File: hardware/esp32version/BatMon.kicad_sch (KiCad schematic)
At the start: 38 parts, among them J1 Battery_Connector, J3 Prog_Connector, J5 Charging_Connector, Q1 Q_PMOS_DDGSDD_TSOP-6, Q1 SS8050-G, Q2 Q_PMOS_DDGSDD_TSOP-6, Q2 SS8050-G, Q3 SS8050-G, SW1 POWER_SW, U1 ESP32-WROOM-32D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

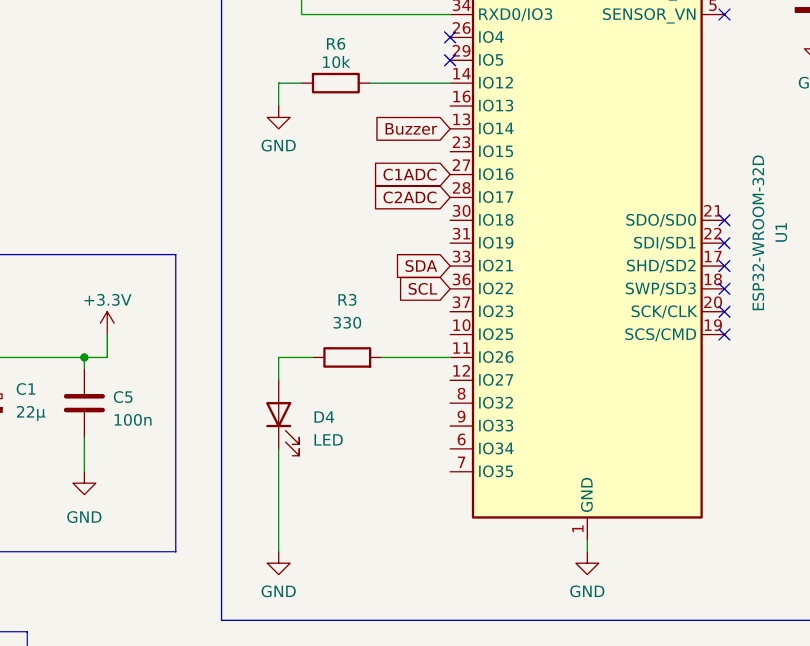
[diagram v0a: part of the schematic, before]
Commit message: fixed battery inputs being connected to non ADC pins on uC (new board revision)
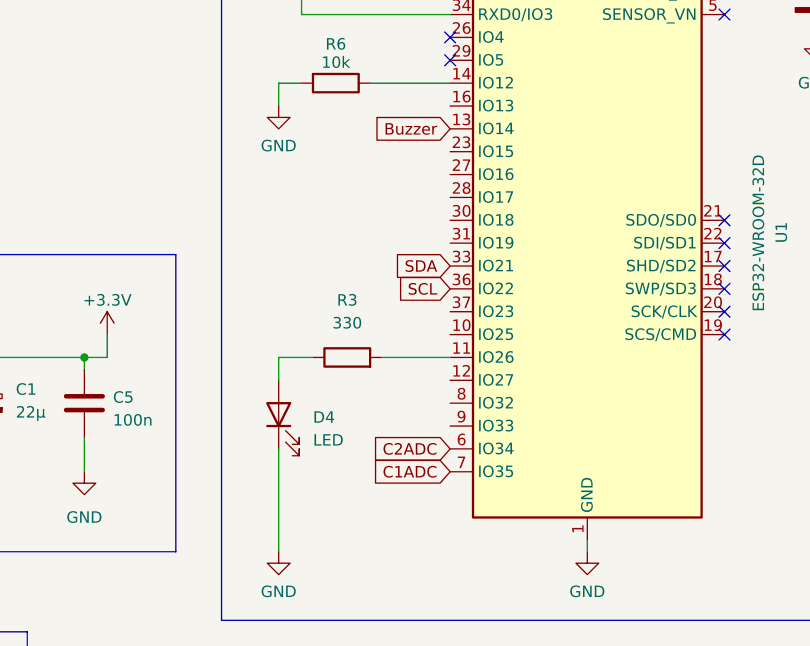
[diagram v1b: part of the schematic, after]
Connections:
- net C1ADC: now also U1.7 (IO35); no longer U1.27 (IO16)
- net C2ADC: now also U1.6 (IO34); no longer U1.28 (IO17)
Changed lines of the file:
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@@
     )
   )
-  (global_label "C2ADC" (shape input) (at 217.17 96.52 180) (fields_autoplaced)
+  (global_label "C2ADC" (shape input) (at 217.17 124.46 180) (fields_autoplaced)
     (effects (font (size 1.27 1.27)) (justify right))
-    (property "Intersheetrefs" "${INTERSHEET_REFS}" (at 208.1561 96.52 0)
+    (property "Intersheetrefs" "${INTERSHEET_REFS}" (at 208.1561 124.46 0)
       (effects (font (size 1.27 1.27)) (justify right) hide)
     )
@@
     )
   )
-  (global_label "C1ADC" (shape input) (at 217.17 93.98 180) (fields_autoplaced)
+  (global_label "C1ADC" (shape input) (at 217.17 127 180) (fields_autoplaced)
     (effects (font (size 1.27 1.27)) (justify right))
-    (property "Intersheetrefs" "${INTERSHEET_REFS}" (at 208.1561 93.98 0)
+    (property "Intersheetrefs" "${INTERSHEET_REFS}" (at 208.1561 127 0)
       (effects (font (size 1.27 1.27)) (justify right) hide)
     )

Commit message: updated programming connector to correct mouser component
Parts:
- J3: Part https://www.mouser.at/ProductDetail/Harwin/M50-3930542?qs=%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 -> https://www.mouser.at/ProductDetail/Harwin/M50-3930642?qs=%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
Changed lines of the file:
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@@
       (effects (font (size 1.27 1.27)) hide)
     )
-    (property "Datasheet" "https://www.mouser.at/ProductDetail/Harwin/M50-3930542?qs=%252BdQmOuGyFcFb1vakt822Tg%3D%3D" (at 226.06 31.75 0)
+    (property "Datasheet" "https://www.mouser.at/ProductDetail/Harwin/M50-3930642?qs=%252BdQmOuGyFcFzM9ygldPnXw%3D%3D" (at 226.06 31.75 0)
       (effects (font (size 1.27 1.27)) hide)
     )
@@
       (effects (font (size 1.27 1.27)) hide)
     )
-    (property "Part" "https://www.mouser.at/ProductDetail/Harwin/M50-3930542?qs=%252BdQmOuGyFcFb1vakt822Tg%3D%3D" (at 226.06 31.75 90)
+    (property "Part" "https://www.mouser.at/ProductDetail/Harwin/M50-3930642?qs=%252BdQmOuGyFcFzM9ygldPnXw%3D%3D" (at 226.06 31.75 90)
       (effects (font (size 1.27 1.27)) hide)
     )
